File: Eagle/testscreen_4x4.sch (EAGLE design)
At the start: 33 parts, among them U1 WS2812, U10 WS2812, U11 WS2812, U12 WS2812, U13 WS2812, U14 WS2812, U15 WS2812, U16 WS2812, U2 WS2812, U3 WS2812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

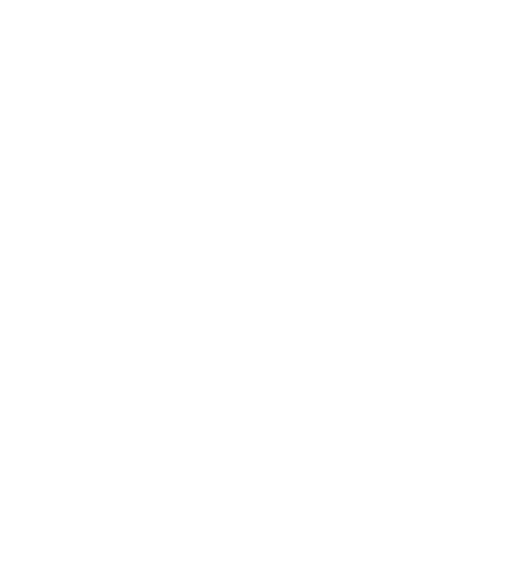
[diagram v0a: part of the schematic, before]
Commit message: developing esp32 version on new branch
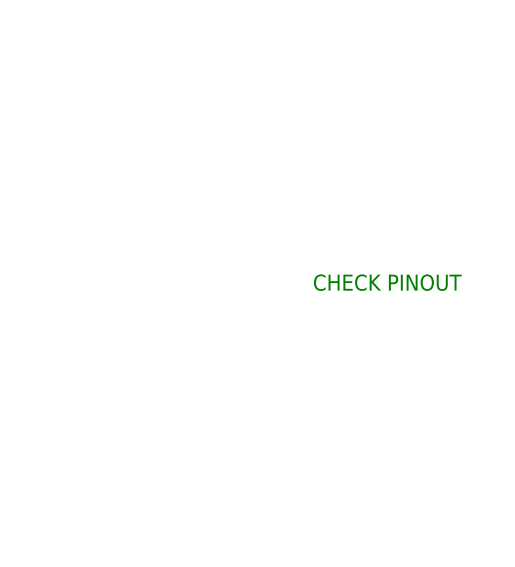
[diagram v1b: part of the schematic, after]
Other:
- note added: "CHECK PINOUT"
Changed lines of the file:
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@@
 <sheet>
 <plain>
+<text x="200.66" y="-15.24" size="1.778" layer="91">CHECK PINOUT</text>
 </plain>
 <instances>
